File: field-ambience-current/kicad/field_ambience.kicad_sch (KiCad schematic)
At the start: 0 parts

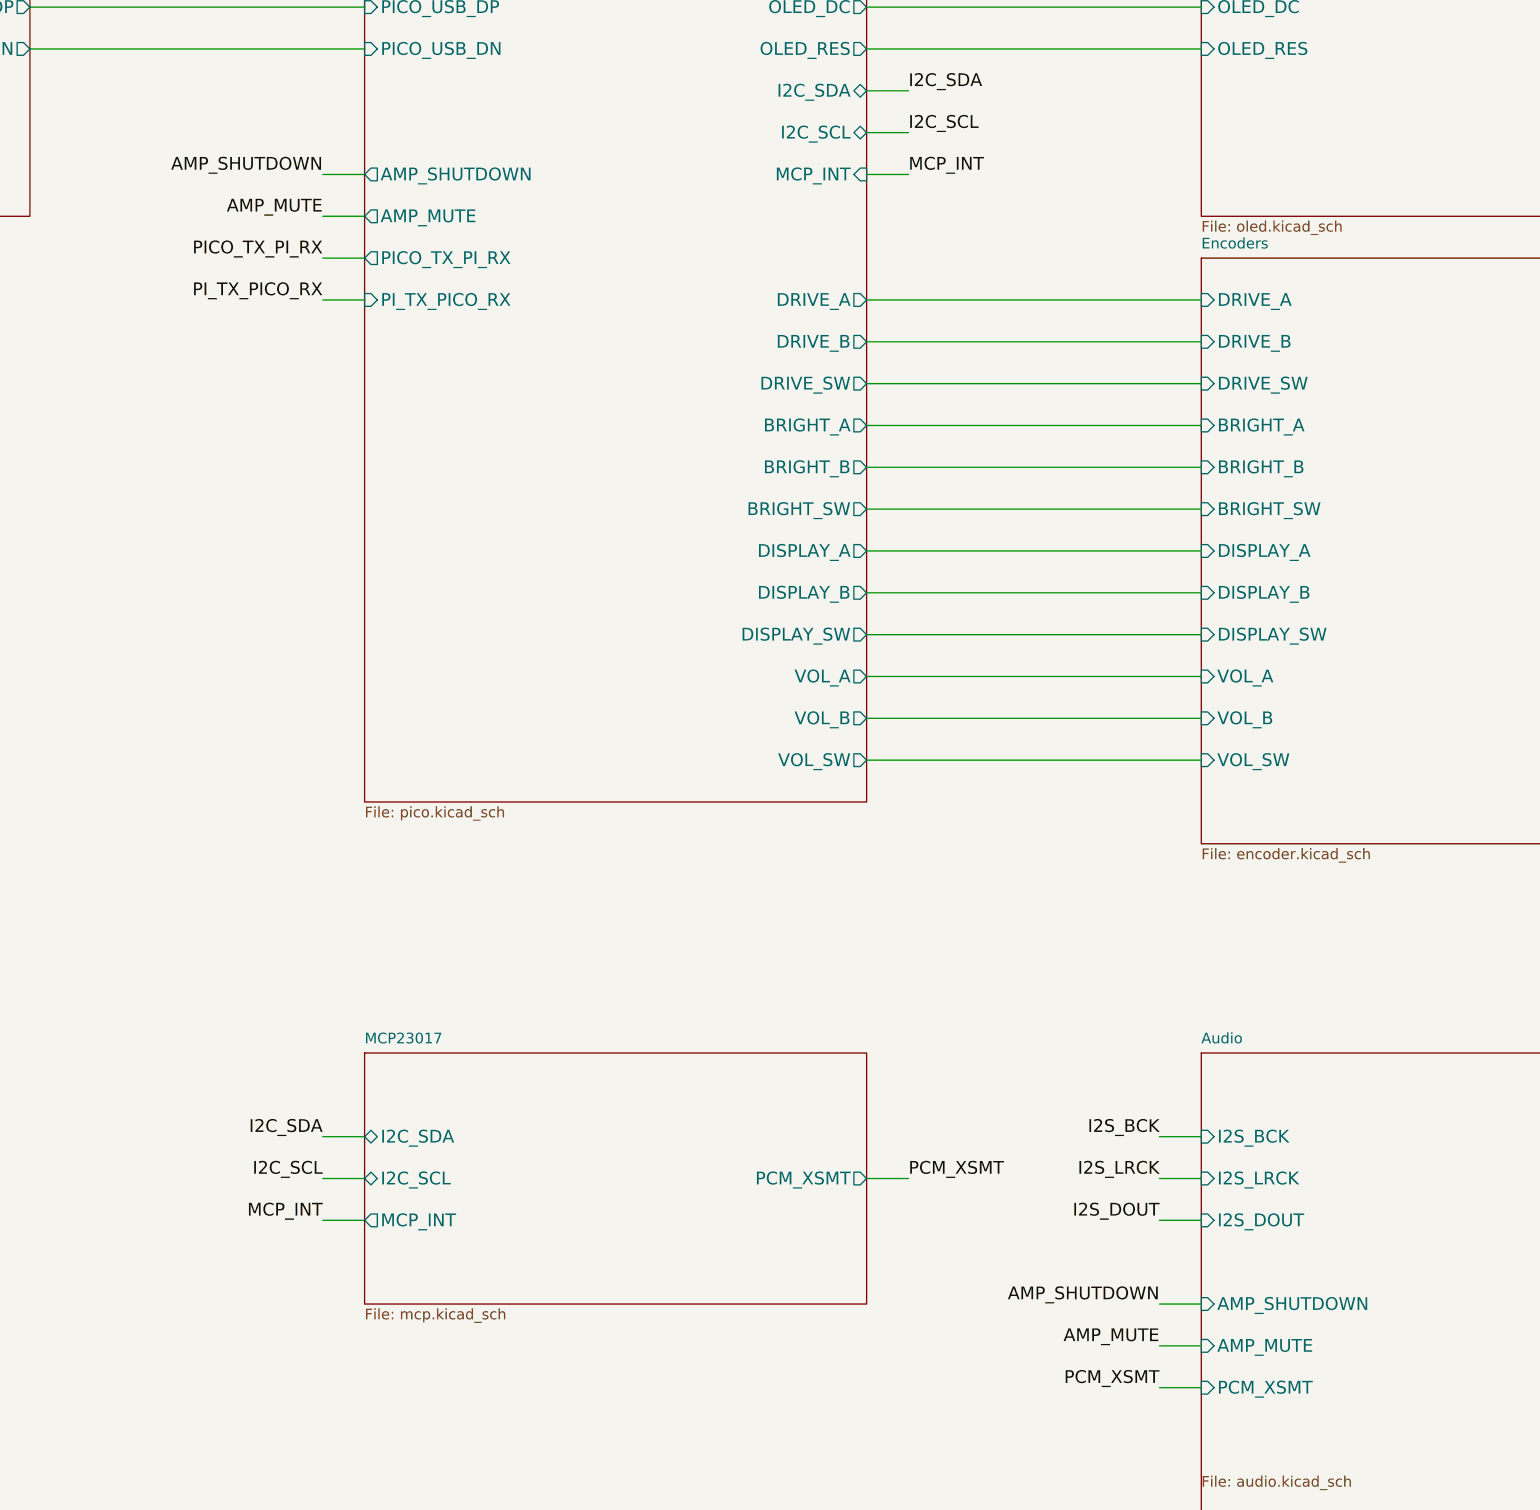
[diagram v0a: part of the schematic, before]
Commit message: v0.6.3-r6: Stabilization pass — PVDD decoupling, startup sequence, SPEC consolidation
No new features. Pure stabilization per senior-engineer review.

=== HIGH fixes ===

1. PAM8403H PVDD decoupling (pins 4, 13) — was missing
   Datasheet (PAM8403H.PDF "Application Information") requires:
   "1.0µF ceramic close to VDD" (HF) + "20µF or greater" (bulk).
   Previous: only C9 10µF + C9b 100nF at VDD (pin 6). PVDD pins 4 (L)
   and 13 (R) had no local decoupling → Class-D 250kHz switching
   transients would modulate PVDD → distortion at volume + EMI.
   Fix:
   - Left (VDD pin6 + PVDD-L pin4): C9 10µF→22µF (C45783), C9b 100nF→1µF
   - Right (PVDD-R pin13): NEW C_PVDDR 22µF + C_PVDDR_HF 1µF local
   Note: corrected my own earlier review — PVDD is pins 4+13 only,
   NOT 4/10/13 (pin 10 is INR input, not power).

2. PAM8403 startup sequence — was in wrong order in SPEC
   SPEC §8 had: /MUTE=HIGH first, then /SHDN=HIGH 100ms later.
   Both are active-LOW. Un-muting before chip wakeup means audio
   passes the instant /SHDN goes HIGH → pop.
   Fix: /SHDN=HIGH first (chip wakes, references settle, output still
   muted via /MUTE=LOW), then /MUTE=HIGH 50ms later. Shutdown reverses.
   Corrected in SPEC §5 AND §8 body (not just errata).

=== SPEC consolidation (single source of truth) ===

- Moved entire Errata-Historie (v0.6.1 → v0.6.3-r5, 327 lines) out of
  SPEC body into new CHANGELOG.md
- SPEC header rewritten: clean rev marker, status "SCHEMATIC IN REVIEW"
- SPEC body now describes ONLY the current state, no errata/old-value
  contradictions
- §3 decoupling table updated: C9 22µF, C9b 1µF, + C_PVDDR/C_PVDDR_HF,
  + C_VREF rows added
- §5 + §8: startup sequence corrected, active-low convention documented

=== Cross-domain fix: AMP signal naming ===

Renamed AMP_SHUTDOWN → AMP_nSHDN, AMP_MUTE → AMP_nMUTE throughout the
generator (17 occurrences). Both PAM8403H /SHDN and /MUTE are active-LOW;
old names implied active-high and were a firmware-bug magnet. SPEC §5
already used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
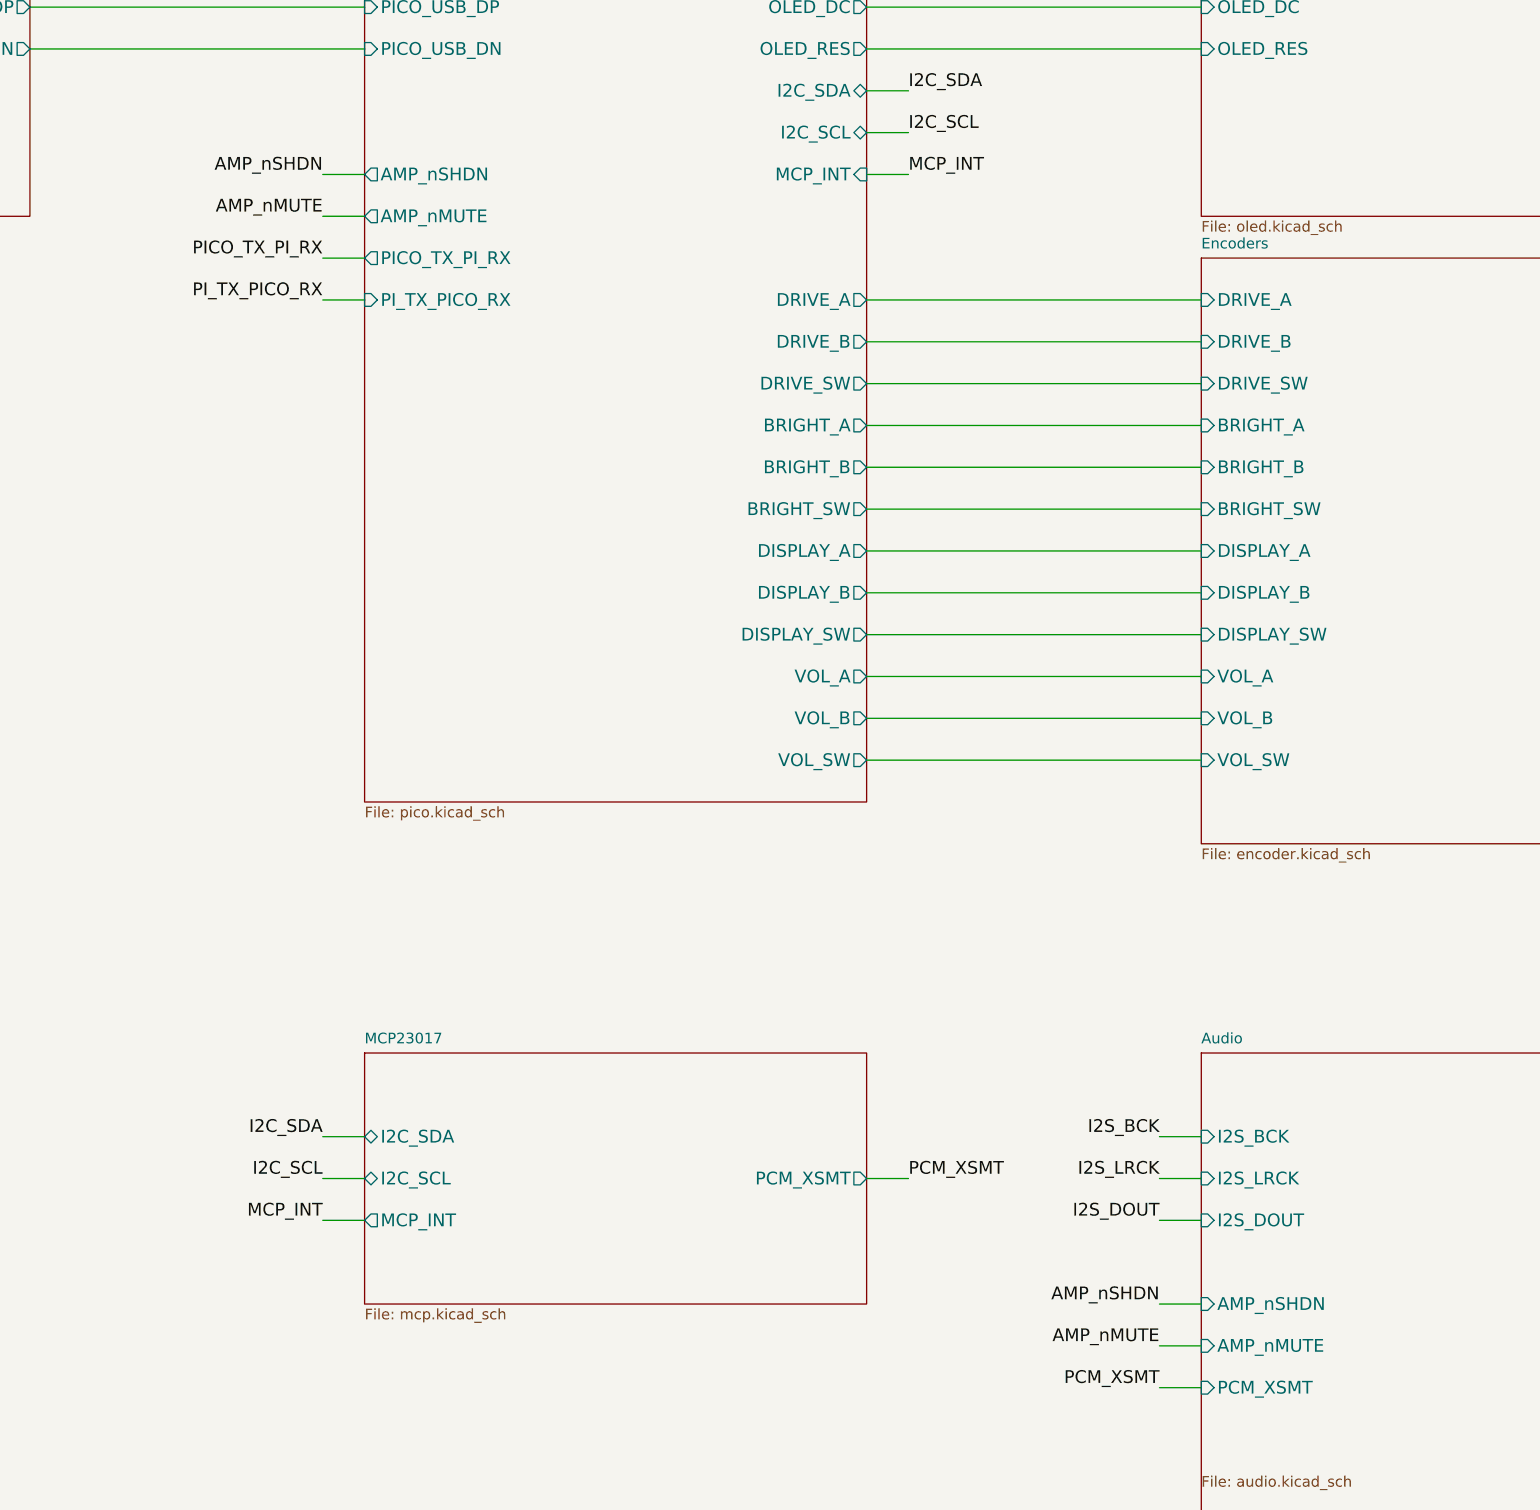
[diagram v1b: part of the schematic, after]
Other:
- sheet Audio ports: added AMP_nMUTE, AMP_nSHDN; removed AMP_MUTE, AMP_SHUTDOWN
- sheet Pico ports: added AMP_nMUTE, AMP_nSHDN; removed AMP_MUTE, AMP_SHUTDOWN
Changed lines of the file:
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@@
       (effects (font (size 1.524 1.524)) (justify right))
 )
-    (pin "AMP_SHUTDOWN" output (at 130 95 180)
+    (pin "AMP_nSHDN" output (at 130 95 180)
       (effects (font (size 1.524 1.524)) (justify left))
 )
-    (pin "AMP_MUTE" output (at 130 100 180)
+    (pin "AMP_nMUTE" output (at 130 100 180)
       (effects (font (size 1.524 1.524)) (justify left))
 )
@@
       (effects (font (size 1.524 1.524)) (justify left))
 )
-    (pin "AMP_SHUTDOWN" input (at 230 230 180)
+    (pin "AMP_nSHDN" input (at 230 230 180)
       (effects (font (size 1.524 1.524)) (justify left))
 )
-    (pin "AMP_MUTE" input (at 230 235 180)
+    (pin "AMP_nMUTE" input (at 230 235 180)
       (effects (font (size 1.524 1.524)) (justify left))
 )
@@
 ))
   (wire (pts (xy 125 95) (xy 130 95)) (stroke (width 0) (type default)))
-  (label "AMP_SHUTDOWN" (at 125 95 0) (effects (font (size 1.524 1.524)) (justify right bottom)))
+  (label "AMP_nSHDN" (at 125 95 0) (effects (font (size 1.524 1.524)) (justify right bottom)))
   (wire (pts (xy 125 100) (xy 130 100)) (stroke (width 0) (type default)))
-  (label "AMP_MUTE" (at 125 100 0) (effects (font (size 1.524 1.524)) (justify right bottom)))
+  (label "AMP_nMUTE" (at 125 100 0) (effects (font (size 1.524 1.524)) (justify right bottom)))
   (wire (pts (xy 225 230) (xy 230 230)) (stroke (width 0) (type default)))
-  (label "AMP_SHUTDOWN" (at 225 230 0) (effects (font (size 1.524 1.524)) (justify right bottom)))
+  (label "AMP_nSHDN" (at 225 230 0) (effects (font (size 1.524 1.524)) (justify right bottom)))
   (wire (pts (xy 225 235) (xy 230 235)) (stroke (width 0) (type default)))
-  (label "AMP_MUTE" (at 225 235 0) (effects (font (size 1.524 1.524)) (justify right bottom)))
+  (label "AMP_nMUTE" (at 225 235 0) (effects (font (size 1.524 1.524)) (justify right bottom)))
   (wire (pts (xy 190 215) (xy 195 215)) (stroke (width 0) (type default)))
   (label "PCM_XSMT" (at 195 215 0) (effects (font (size 1.524 1.524)) (justify left bottom)))

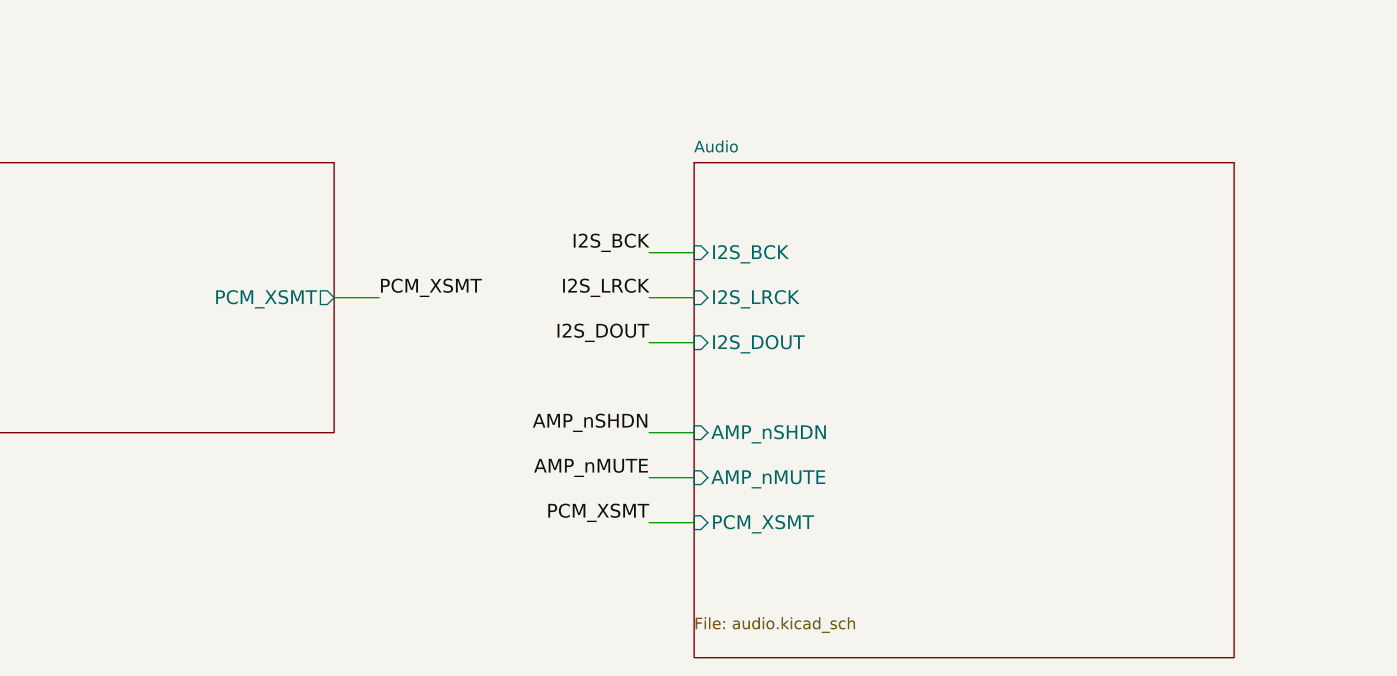
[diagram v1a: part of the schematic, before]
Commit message: v0.7-pre: Choc V2 footprint fix + Line-Out/Headphone block (J8)
Two real design improvements requested after the device evaluation.

=== 1. Switch footprint mismatch fixed (Choc V2) ===

BUG: generator referenced Button_Switch_Keyboard:SW_Hotswap_Kailh_MX_*
(MX hotswap) while BOM/SPEC specify Kailh Choc V2 throughout. MX and
Choc V2 are physically incompatible (pin spacing, height, keycap stem).
Building the MX footprint with Choc V2 sockets → parts don't fit.

FIX: footprints → Switch_Keyboard_Hotswap_Kailh:SW_Hotswap_Kailh_Choc_V1V2_*
(1.00u modifiers, 2.00u cells). Verified: 0 MX refs remain, 10 Choc refs.

LIBRARY: these are NOT in KiCad standard libs. Requires the kiswitch
keyswitch-kicad-library (PCM → Libraries → "Keyswitch Kicad Library").
Documented in SPEC §4, PCB_TODO B0, CHANGELOG. Exact footprint name must
be verified after install (B0 blocker).

=== 2. Line-Out / Headphone block (J8) — fixes the "deep character" problem ===

The 40mm onboard speakers physically cannot reproduce the 30-60Hz SubBass
the Sound Constitution is built around. Without an external output the
device's core character stays trapped in the box.

Hardware (Sheet 6 audio extended):
- J8: 3.5mm TRS jack with insertion-detect switch (PJ-320 class, C2884109)
- Passive tap from PCM5102A VOUTL/VOUTR BEFORE the PAM8403. PCM5102A output
  is ground-centered (internal charge pump) → no coupling caps needed.
- R_LO_L / R_LO_R: 22Ω series (short-circuit protection, C22962)
- Jack-detect: J8 DET switch → MCP23017 GPA6 (pull-up + IRQ enabled).
  Idle (no plug) = LOW, inserted = HIGH.

Firmware:
- New AudioPower.speakers(on) method separates speaker-amp mute from full
  system mute. Jack insert → mute ONLY the PAM8403; PCM5102A DAC + line-out
  stay live. Speaker and line-out are mutually exclusive (plug = speakers off).
- read_buttons() now reads GPA6, tracks jack state, emits {"event":"jack",
  "inserted":bool}, calls amp.speakers(not inserted) locally.
- {"set":"amp"} command now calls speake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
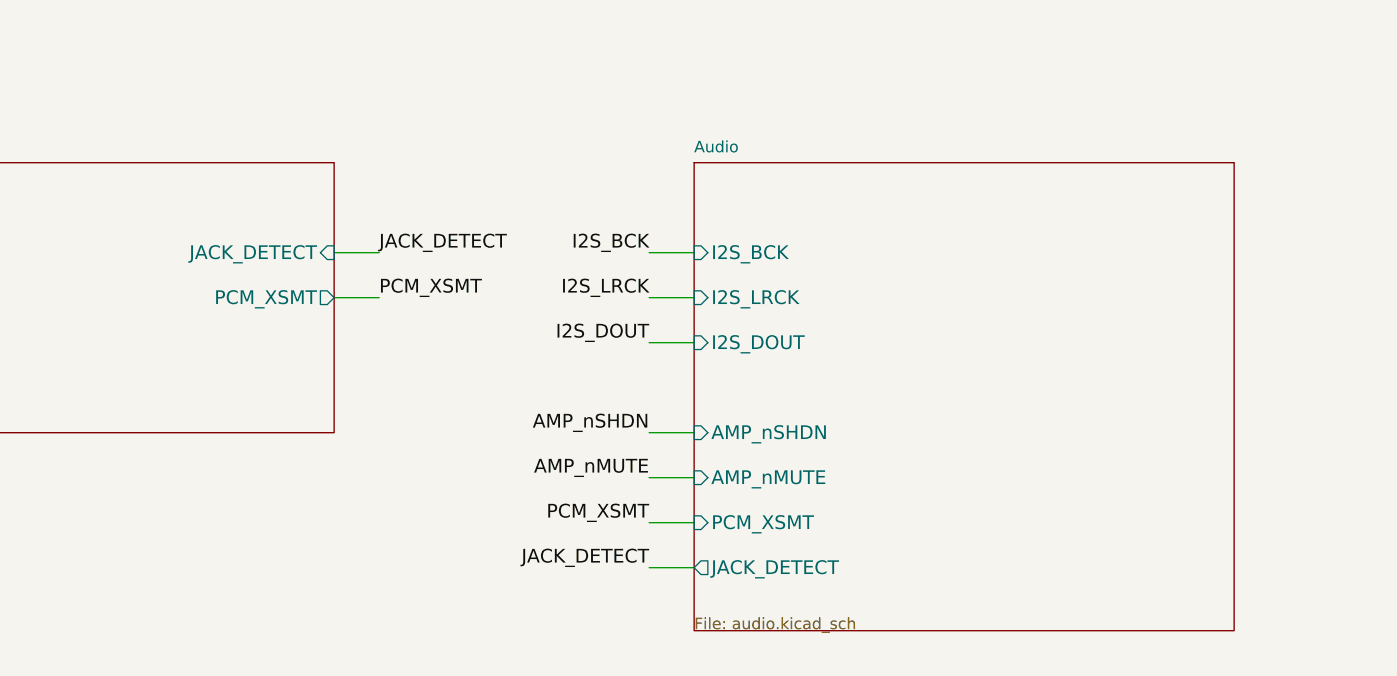
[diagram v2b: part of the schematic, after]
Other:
- sheet Audio ports: added JACK_DETECT; removed none
- sheet MCP23017 ports: added JACK_DETECT; removed none
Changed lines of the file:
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@@
     (pin "PCM_XSMT" output (at 190 215 0)
+      (effects (font (size 1.524 1.524)) (justify right))
+)
+    (pin "JACK_DETECT" input (at 190 210 0)
       (effects (font (size 1.524 1.524)) (justify right))
 ))
@@
   (wire (pts (xy 325 75) (xy 330 75)) (stroke (width 0) (type default)))
   (label "I2S_DOUT" (at 325 75 0) (effects (font (size 1.524 1.524)) (justify right bottom)))
-  (sheet (at 230 200) (size 60 55) (fields_autoplaced)
+  (sheet (at 230 200) (size 60 52) (fields_autoplaced)
     (stroke (width 0.1524) (type solid))
     (fill (color 0 0 0 0.0000))
@@
     (pin "PCM_XSMT" input (at 230 240 180)
       (effects (font (size 1.524 1.524)) (justify left))
+)
+    (pin "JACK_DETECT" output (at 230 245 180)
+      (effects (font (size 1.524 1.524)) (justify left))
 ))
   (wire (pts (xy 125 95) (xy 130 95)) (stroke (width 0) (type default)))
@@
   (wire (pts (xy 225 240) (xy 230 240)) (stroke (width 0) (type default)))
   (label "PCM_XSMT" (at 225 240 0) (effects (font (size 1.524 1.524)) (justify right bottom)))
+  (wire (pts (xy 190 210) (xy 195 210)) (stroke (width 0) (type default)))
+  (label "JACK_DETECT" (at 195 210 0) (effects (font (size 1.524 1.524)) (justify left bottom)))
+  (wire (pts (xy 225 245) (xy 230 245)) (stroke (width 0) (type default)))
+  (label "JACK_DETECT" (at 225 245 0) (effects (font (size 1.524 1.524)) (justify right bottom)))
   (wire (pts (xy 225 210) (xy 230 210)) (stroke (width 0) (type default)))
   (label "I2S_BCK" (at 225 210 0) (effects (font (size 1.524 1.524)) (justify right bottom)))
